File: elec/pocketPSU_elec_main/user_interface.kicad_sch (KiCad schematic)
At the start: 25 parts, among them J3 Conn_01x12_Pin, SW1 EC11E09244BS, U1 2N7002_C5224215

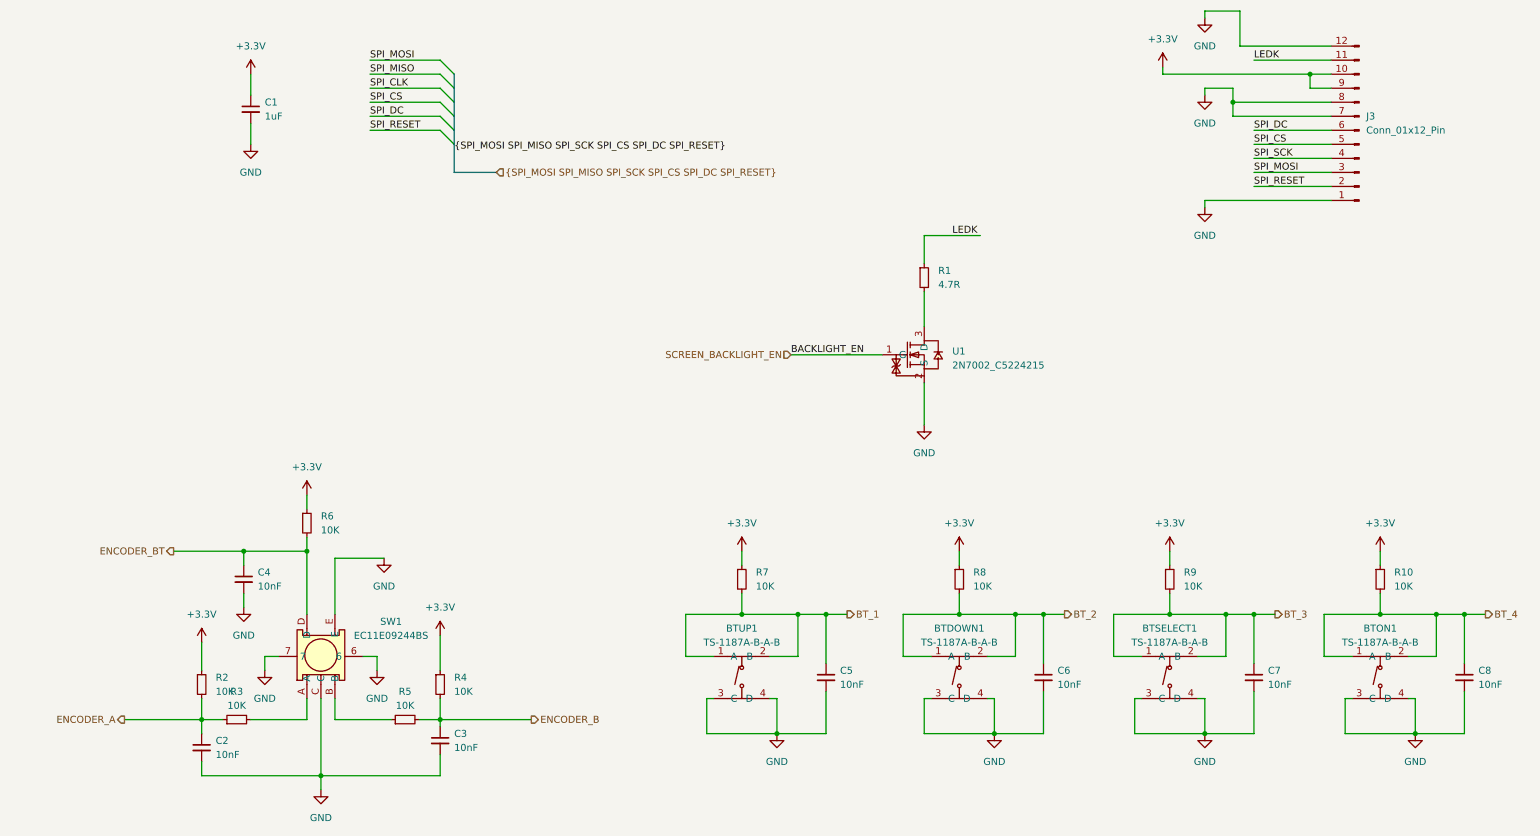
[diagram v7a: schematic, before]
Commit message: add copper fill
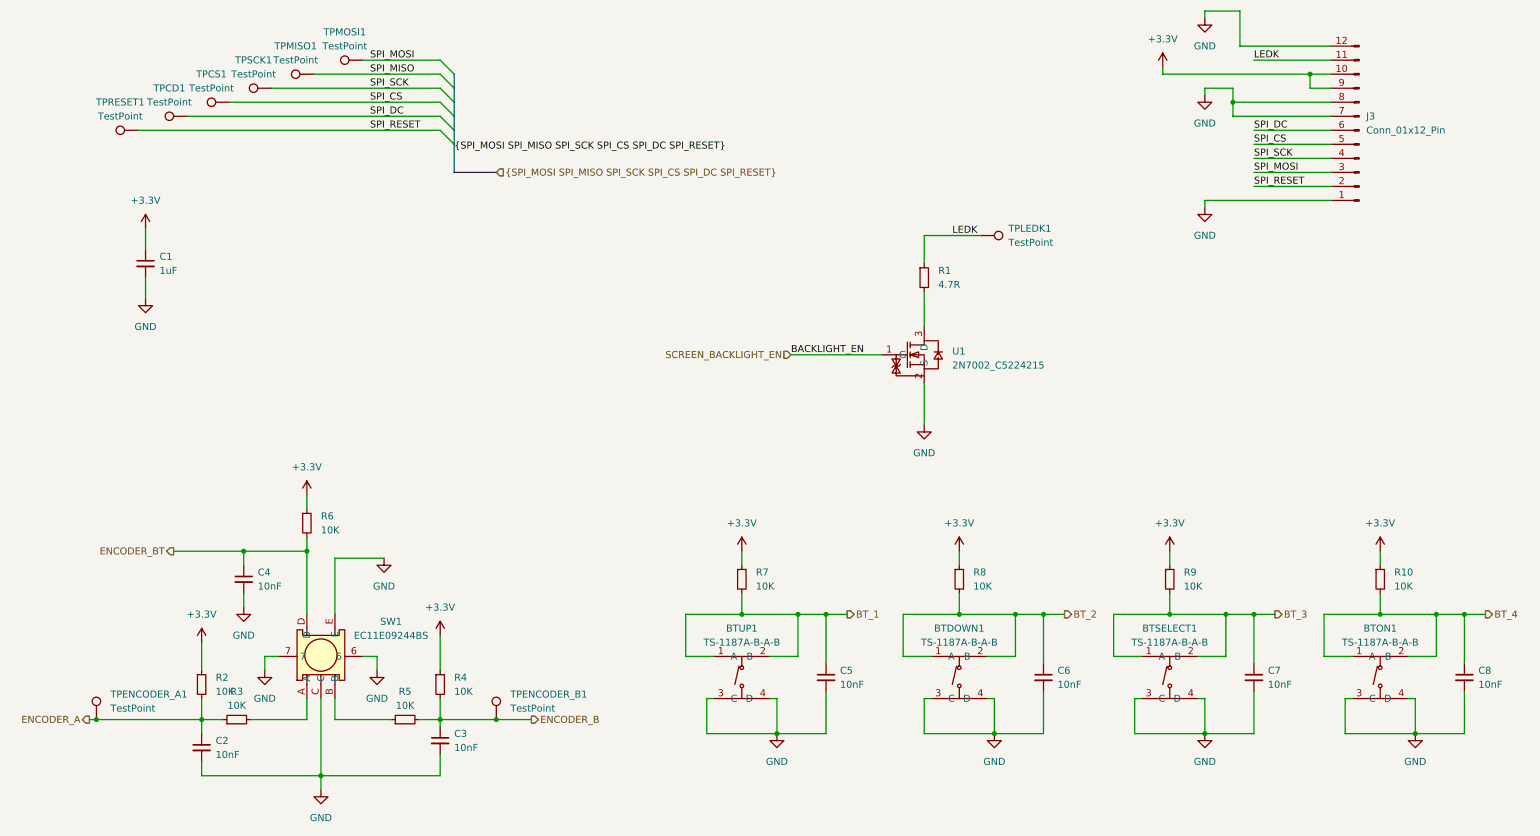
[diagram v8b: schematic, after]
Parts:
- added TPCD1, TPCS1, TPENCODER_A1, TPENCODER_B1, TPLEDK1, TPMISO1, TPMOSI1, TPRESET1, TPSCK1: TestPoint, TestPoint:TestPoint_Pad_D1.5mm, symbol Connector:TestPoint
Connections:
- net ENCODER_A: now also TPENCODER_A1.1
- net ENCODER_B: now also TPENCODER_B1.1
- net LEDK: now also TPLEDK1.1
- net SPI_CS: now also TPCS1.1
- net SPI_DC: now also TPCD1.1
- net SPI_MISO: now also TPMISO1.1
- net SPI_MOSI: now also TPMOSI1.1
- net SPI_RESET: now also TPRESET1.1
- net SPI_SCK: now also TPSCK1.1
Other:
- moved on the sheet: C1
